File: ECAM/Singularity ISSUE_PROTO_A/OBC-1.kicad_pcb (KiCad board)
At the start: 6 copper layers, 42.8 x 42.8 mm, 110 parts, among them J1 ERM8-020-X, J2 ERF6-020-X, J3 Conn_01x02_Female, Q1 MGSF1N02L, Q2 MGSF1N02L, U1 TPS62850x-Q1, U10 FM33256B, U11 TMS5701227CZWTQQ1, U2 TPS62850x-Q1, U3 LTC4353, U4 SN65HVD230M-EP, U5 SN65HVD230M-EP, U6 SN65HVD230M-EP, U7 CY15B108QI, U8 S70FL01GS, X1 ASTMTXK-32.768KHZ

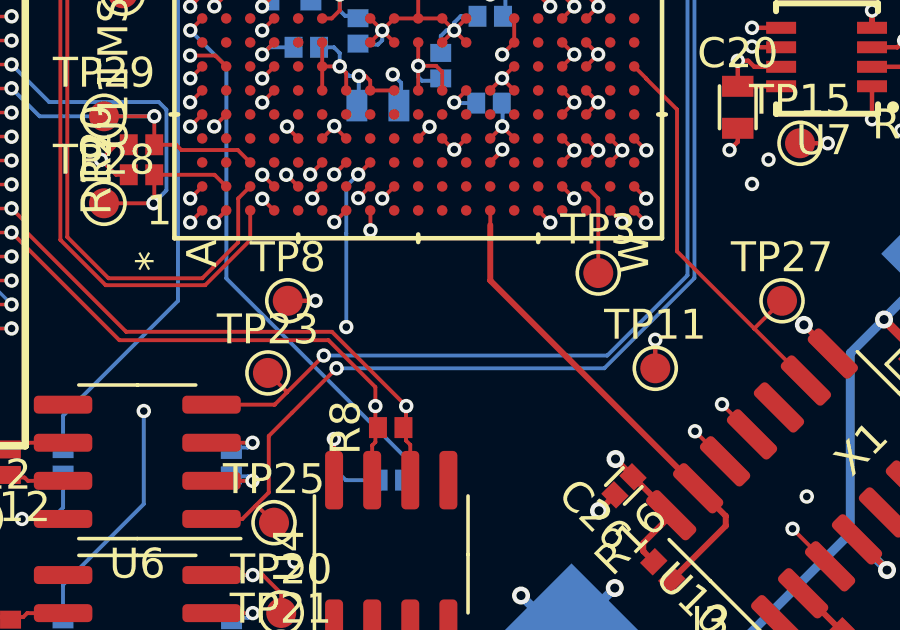
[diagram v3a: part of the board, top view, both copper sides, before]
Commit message: added uC XTAL, routed ground stitching and power plane
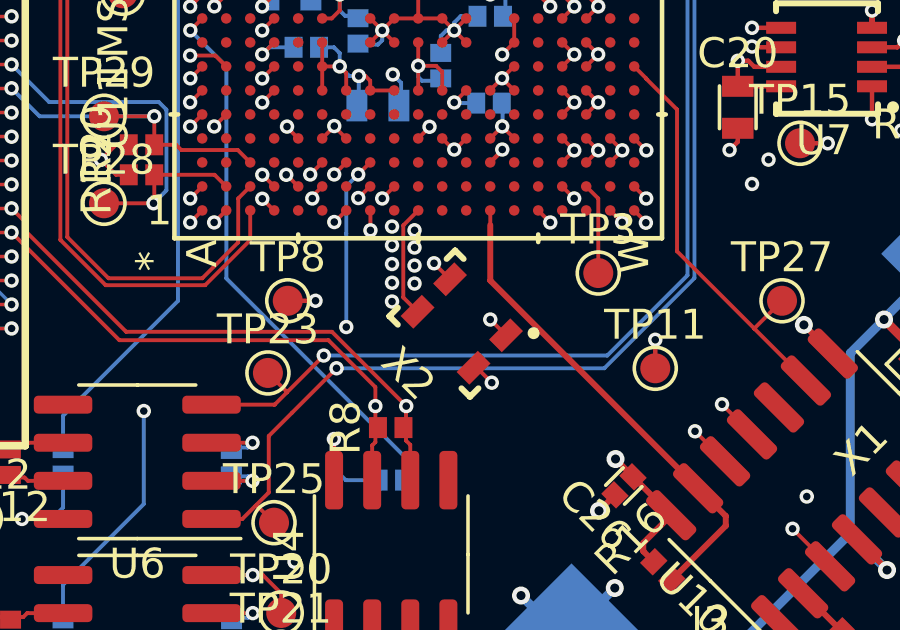
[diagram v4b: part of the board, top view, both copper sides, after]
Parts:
- added X2: LFTCXO075797, TFT_XTAL:LFTCXO075797, F.Cu at (113.2, 100.7)
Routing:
- net /TMS570_uC/uC_OSC_IN: track 0.00 -> 3.78 mm
- net GND: track 205.0 -> 206.5 mm, vias 182 -> 193
- net OBC_3V3: track 102.9 -> 102.7 mm, vias 33 -> 34
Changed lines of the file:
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@@
     (thickness 1.6)
     (drawings 8)
-    (tracks 1751)
+    (tracks 1769)
     (zones 0)
-    (modules 110)
+    (modules 111)
     (nets 223)
   )
@@
     (add_net PAYLOAD_5V)
   )
+  (module TFT_XTAL:LFTCXO075797 (layer F.Cu)
+    (at 113.175 100.7 135)
+    (fp_text reference X2 (at 1.4 -3.2 135) (layer F.SilkS)
+      (effects (font (size 1 1) (thickness 0.15)))
+    )
+    (fp_text value LFTCXO075797 (at 0 -0.5 135) (layer F.Fab)
+      (effects (font (size 1 1) (thickness 0.15)))
+    )
+    (fp_line (start -0.5 0.7) (end 3.1 0.7) (layer F.CrtYd) (width 0.12))
+    (fp_line (start 3.1 0.7) (end 3.1 -2.2) (layer F.CrtYd) (width 0.12))
+    (fp_line (start 3.1 -2.2) (end -0.5 -2.2) (layer F.CrtYd) (width 0.12))
+    (fp_line (start -0.5 -2.2) (end -0.5 0.7) (layer F.CrtYd) (width 0.12))
+    (fp_line (start -0.6 -1.9) (end -0.6 -2.3) (layer F.SilkS) (width 0.2))
+    (fp_line (start -0.6 -2.3) (end -0.2 -2.3) (layer F.SilkS) (width 0.2))
+    (fp_line (start 2.8 -2.3) (end 3.2 -2.3) (layer F.SilkS) (width 0.2))
+    (fp_line (start 3.2 -2.3) (end 3.2 -1.9) (layer F.SilkS) (width 0.2))
+    (fp_line (start 3.2 0.4) (end 3.2 0.8) (layer F.SilkS) (width 0.2))
+    (fp_line (start 3.2 0.8) (end 2.8 0.8) (layer F.SilkS) (width 0.2))
+    (fp_circle (center -0.6 0.7) (end -0.6 0.6) (layer F.SilkS) (width 0.2))
+    (pad 4 smd rect (at 0 -1.53 135) (size 0.6 1) (layers F.Cu F.Paste F.Mask)
+      (net 1 OBC_3V3) (solder_paste_margin_ratio -0.05))
+    (pad 3 smd rect (at 2.64 -1.53 135) (size 0.6 1) (layers F.Cu F.Paste F.Mask)
+      (net 111 /TMS570_uC/uC_OSC_IN) (solder_paste_margin_ratio -0.05))
+    (pad 2 smd rect (at 2.64 0 135) (size 0.6 1) (layers F.Cu F.Paste F.Mask)
+      (net 2 GND) (solder_paste_margin_ratio -0.05))
+    (pad 1 smd rect (at 0 0 135) (size 0.6 1) (layers F.Cu F.Paste F.Mask)
+      (net 2 GND) (solder_paste_margin_ratio -0.05))
+  )
   (module TFT_GQFN:CY15B108QI (layer F.Cu)
     (at 125.375 92.4 180)
@@
   (gr_arc (start 128.7 111.3) (end 128.7 114.3) (angle -90) (layer Edge.Cuts) (width 0.2))
   (gr_line (start 91.9 114.3) (end 128.7 114.3) (layer Edge.Cuts) (width 0.2))
+  (via (at 109.375 97.075) (size 0.48) (drill 0.25) (layers F.Cu B.Cu) (net 2))
+  (via (at 109.375 97.7) (size 0.48) (drill 0.25) (layers F.Cu B.Cu) (net 2))
+  (via (at 109.375 98.325) (size 0.48) (drill 0.25) (layers F.Cu B.Cu) (net 2))
+  (via (at 109.375 98.95) (size 0.48) (drill 0.25) (layers F.Cu B.Cu) (net 2))
+  (via (at 109.375 99.575) (size 0.48) (drill 0.25) (layers F.Cu B.Cu) (net 2))
+  (via (at 110.125 98.975) (size 0.48) (drill 0.25) (layers F.Cu B.Cu) (net 2))
+  (via (at 110.125 98.375) (size 0.48) (drill 0.25) (layers F.Cu B.Cu) (net 2))
+  (via (at 110.125 97.775) (size 0.48) (drill 0.25) (layers F.Cu B.Cu) (net 2))
+  (via (at 110.125 97.2) (size 0.48) (drill 0.25) (layers F.Cu B.Cu) (net 2))
   (via (at 107.63152 91.73894) (size 0.48) (drill 0.25) (layers F.Cu B.Cu) (net 1))
   (segment (start 107.63122 91.73864) (end 107.63152 91.73894) (width 0.13) (layer F.Cu) (net 1))
@@
   (segment (start 117.75 107.625) (end 118.677153 106.697847) (width 0.2) (layer F.Cu) (net 1))
   (segment (start 118.09948 108.24948) (end 117.75 107.9) (width 0.2) (layer F.Cu) (net 1))
-  (segment (start 116.160967 104.160967) (end 116.825 104.825) (width 0.1) (layer In2.Cu) (net 1))
   (segment (start 95.1 79.425) (end 95.1 78.35) (width 0.15) (layer F.Cu) (net 1))
   (via (at 124.249988 82.825) (size 0.48) (drill 0.25) (layers F.Cu B.Cu) (net 1))
@@
   (segment (start 126.22 91.1) (end 126.445 90.875) (width 0.15) (layer F.Cu) (net 1))
   (segment (start 125.375 91.1) (end 126.22 91.1) (width 0.15) (layer F.Cu) (net 1))
+  (via (at 112.7 102.279967) (size 0.48) (drill 0.25) (layers F.Cu B.Cu) (net 1))
+  (segment (start 112.201906 101.781873) (end 112.7 102.279967) (width 0.13) (layer F.Cu) (net 1))
+  (segment (start 112.093127 101.781873) (end 112.201906 101.781873) (width 0.13) (layer F.Cu) (net 1))
   (segment (start 106.24772 94.13864) (end 106.24772 94.139607) (width 0.13) (layer F.Cu) (net 2))
   (via (at 109.04884 90.53752) (size 0.48) (drill 0.25) (layers F.Cu B.Cu) (net 2))
@@
   (segment (start 106.24792 94.138441) (end 105.874826 93.765347) (width 0.13) (layer F.Cu) (net 2))
   (via (at 105.874826 93.743717) (size 0.48) (drill 0.25) (layers F.Cu B.Cu) (net 2))
+  (via (at 110.775 98.3) (size 0.48) (drill 0.25) (layers F.Cu B.Cu) (net 2))
+  (segment (start 111.308238 98.833238) (end 110.775 98.3) (width 0.13) (layer F.Cu) (net 2))
+  (via (at 112.65 100.175) (size 0.48) (drill 0.25) (layers F.Cu B.Cu) (net 2))
+  (segment (start 113.175 100.7) (end 112.65 100.175) (width 0.13) (layer F.Cu) (net 2))
   (segment (start 90.297 79.4367) (end 90.3079 79.4258) (width 0.2) (layer B.Cu) (net 3))
   (segment (start 90.3061 79.4258) (end 90.297 79.4349) (width 0.2) (layer F.Cu) (net 3))
@@
   (via (at 113.05 94.508429) (size 0.48) (drill 0.25) (layers F.Cu B.Cu) (net 99))
   (segment (start 110.24792 96.538439) (end 110.246925 96.538439) (width 0.13) (layer F.Cu) (net 111))
+  (segment (start 110.226365 99.915111) (end 109.75 99.438746) (width 0.13) (layer F.Cu) (net 111))
+  (segment (start 109.75 97.036359) (end 110.24792 96.538439) (width 0.13) (layer F.Cu) (net 111))
+  (segment (start 109.75 99.438746) (end 109.75 97.036359) (width 0.13) (layer F.Cu) (net 111))
   (segment (start 109.44792 82.138441) (end 109.4489 82.138441) (width 0.13) (layer F.Cu) (net 112))
   (via (at 109.45 80.918799) (size 0.48) (drill 0.25) (layers F.Cu B.Cu) (net 112))
@@
         (xy 98.15 94.4) (xy 100.15 94.4) (xy 100.15 95.3) (xy 98.15 95.3) (xy 98.15 101.76245)
         (xy 99.9 103.75) (xy 105.4 103.725) (xy 105.4 105.025) (xy 99.9 105.05) (xy 99.9 106.8)
-        (xy 102.4 109.55) (xy 109.9 109.55) (xy 115.65 104.05) (xy 117.4 104.05) (xy 117.4 105.3)
-        (xy 115.65 105.3) (xy 110.65 110.3) (xy 110.65 112.3) (xy 109.15 112.3) (xy 109.15 110.55)
-        (xy 101.9 110.55) (xy 98.9 107.3) (xy 98.9 103.8) (xy 97.15 102.05) (xy 97.15 86.55)
-        (xy 94.15 86.55) (xy 94.15 73.3) (xy 96.9 73.3) (xy 96.9 77.55) (xy 110.4 77.55)
-        (xy 110.4 73.8) (xy 112.9 73.8) (xy 112.9 75.05) (xy 111.4 75.05) (xy 111.4 77.55)
-        (xy 123.9 77.55) (xy 123.9 74.55) (xy 126.4 74.55) (xy 126.4 78.8) (xy 122.9 78.8)
-        (xy 122.9 82.3) (xy 124.65 82.3) (xy 124.65 83.3) (xy 122.9 83.3) (xy 122.9 88.8)
-        (xy 126.9 88.8) (xy 126.9 91.3) (xy 125.9 91.3) (xy 125.9 89.55) (xy 121.4 89.55)
-        (xy 121.4 92.05) (xy 120.4 92.05) (xy 120.4 88.8) (xy 122.15 88.8) (xy 122.15 83.3)
-        (xy 122.15 78.8) (xy 105.4 78.8) (xy 105.4 81.8) (xy 107.15 83.55) (xy 107.15 84.55)
-        (xy 107.9 85.3) (xy 109.9 85.3) (xy 110.4 85.8) (xy 112.9 85.8) (xy 113.4 86.3)
-        (xy 113.4 92.8) (xy 112.9 93.3) (xy 111.15 93.3) (xy 110.4 92.55) (xy 108.65 92.55)
-        (xy 107.65 92.55) (xy 106.9 91.8) (xy 106.9 86.55) (xy 106.9 85.3) (xy 106.4 84.8)
-        (xy 106.4 83.8) (xy 104.65 82.05) (xy 104.65 78.8) (xy 95.9 78.8) (xy 95.9 84.8)
-        (xy 98.15 84.8)
+        (xy 102.4 109.55) (xy 109.9 109.55) (xy 114.575 105.025) (xy 114.57618 104.773843) (xy 112.05 102.2)
+        (xy 112.575 101.675) (xy 115.425 104.425) (xy 117.4 104.4) (xy 117.4 105.3) (xy 115.45 105.3)
+        (xy 110.65 110) (xy 110.65 112.3) (xy 109.15 112.3) (xy 109.15 110.55) (xy 101.9 110.55)
+        (xy 98.9 107.3) (xy 98.9 103.8) (xy 97.15 102.05) (xy 97.15 86.55) (xy 94.15 86.55)
+        (xy 94.15 73.3) (xy 96.9 73.3) (xy 96.9 77.55) (xy 110.4 77.55) (xy 110.4 73.8)
+        (xy 112.9 73.8) (xy 112.9 75.05) (xy 111.4 75.05) (xy 111.4 77.55) (xy 123.9 77.55)
+        (xy 123.9 74.55) (xy 126.4 74.55) (xy 126.4 78.8) (xy 122.9 78.8) (xy 122.9 82.3)
+        (xy 124.65 82.3) (xy 124.65 83.3) (xy 122.9 83.3) (xy 122.9 88.8) (xy 126.9 88.8)
+        (xy 126.9 91.3) (xy 125.9 91.3) (xy 125.9 89.55) (xy 121.4 89.55) (xy 121.4 92.05)
+        (xy 120.4 92.05) (xy 120.4 88.8) (xy 122.15 88.8) (xy 122.15 83.3) (xy 122.15 78.8)
+        (xy 105.4 78.8) (xy 105.4 81.8) (xy 107.15 83.55) (xy 107.15 84.55) (xy 107.9 85.3)
+        (xy 109.9 85.3) (xy 110.4 85.8) (xy 112.9 85.8) (xy 113.4 86.3) (xy 113.4 92.8)
+        (xy 112.9 93.3) (xy 111.15 93.3) (xy 110.4 92.55) (xy 108.65 92.55) (xy 107.65 92.55)
+        (xy 106.9 91.8) (xy 106.9 86.55) (xy 106.9 85.3) (xy 106.4 84.8) (xy 106.4 83.8)
+        (xy 104.65 82.05) (xy 104.65 78.8) (xy 95.9 78.8) (xy 95.9 84.8) (xy 98.15 84.8)
       )
     )
